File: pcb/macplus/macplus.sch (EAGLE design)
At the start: 9 parts, among them J1 ATX24RH

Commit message: mac plus adaptor pretty much done
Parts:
- added JP3: (no value), pinhead:PINHD-1X2
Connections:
- net GND: now also JP3.2
- net N$10: now also JP3.1
- net N$6: no longer J1.5V@0
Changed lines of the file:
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@@
 <part name="P+5" library="supply1" library_urn="urn:adsk.eagle:library:371" deviceset="+12V" device=""/>
 <part name="P+6" library="supply1" library_urn="urn:adsk.eagle:library:371" deviceset="+5V" device=""/>
+<part name="JP3" library="pinhead" library_urn="urn:adsk.eagle:library:325" deviceset="PINHD-1X2" device="" package3d_urn="urn:adsk.eagle:package:22435/2"/>
+<part name="GND5" library="supply1" library_urn="urn:adsk.eagle:library:371" deviceset="GND" device=""/>
 </parts>
 <sheets>
@@
 <attribute name="VALUE" x="22.86" y="96.52" size="1.778" layer="96" rot="R90"/>
 </instance>
+<instance part="JP3" gate="G$1" x="165.1" y="78.74" smashed="yes">
+<attribute name="NAME" x="158.75" y="84.455" size="1.778" layer="95"/>
+<attribute name="VALUE" x="158.75" y="73.66" size="1.778" layer="96"/>
+</instance>
+<instance part="GND5" gate="1" x="177.8" y="73.66" smashed="yes">
+<attribute name="VALUE" x="175.26" y="71.12" size="1.778" layer="96"/>
+</instance>
 </instances>
 <busses>
@@
 <pinref part="U$3" gate="G$1" pin="11_VBATT"/>
 <wire x1="43.18" y1="81.28" x2="116.84" y2="81.28" width="0.1524" layer="91"/>
+<pinref part="JP3" gate="G$1" pin="1"/>
+<wire x1="116.84" y1="81.28" x2="162.56" y2="81.28" width="0.1524" layer="91"/>
+<junction x="116.84" y="81.28"/>
 </segment>
 </net>
@@
 <wire x1="-17.78" y1="99.06" x2="-27.94" y2="99.06" width="0.1524" layer="91"/>
 </segment>
+<segment>
+<pinref part="GND5" gate="1" pin="GND"/>
+<pinref part="JP3" gate="G$1" pin="2"/>
+<wire x1="177.8" y1="76.2" x2="177.8" y2="78.74" width="0.1524" layer="91"/>
+<wire x1="177.8" y1="78.74" x2="162.56" y2="78.74" width="0.1524" layer="91"/>
+</segment>
 </net>
 <net name="-12V" class="0">
@@
 <wire x1="68.58" y1="185.42" x2="68.58" y2="187.96" width="0.1524" layer="91"/>
 <junction x="68.58" y="187.96"/>
-<pinref part="J1" gate="G$1" pin="5V@0"/>
-<wire x1="81.28" y1="182.88" x2="68.58" y2="182.88" width="0.1524" layer="91"/>
-<wire x1="68.58" y1="182.88" x2="68.58" y2="185.42" width="0.1524" layer="91"/>
-<junction x="68.58" y="185.42"/>
 <pinref part="U$8" gate="G$1" pin="B0"/>
 <pinref part="U$8" gate="G$1" pin="B1"/>

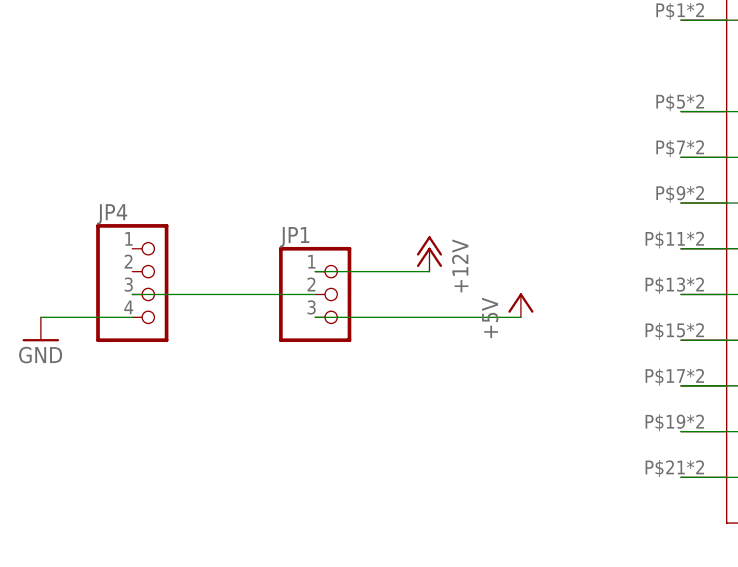
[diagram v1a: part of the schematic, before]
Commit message: updated mac plus atx adaptor
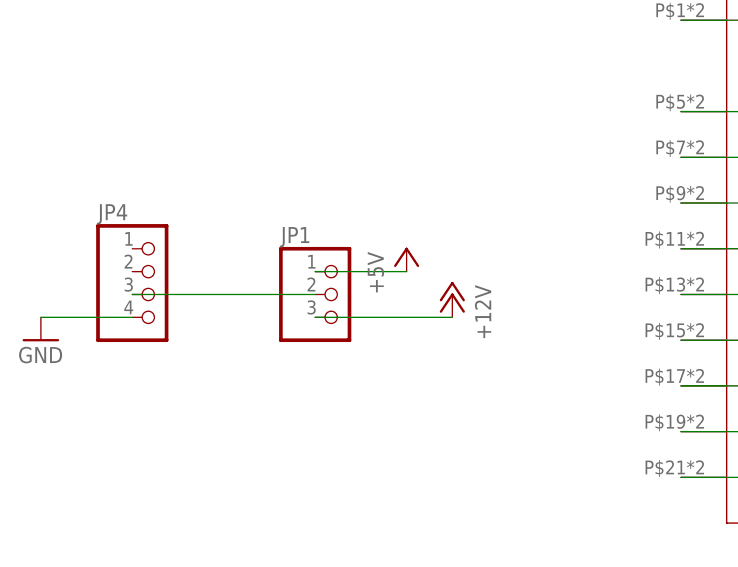
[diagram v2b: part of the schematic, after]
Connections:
- net +12V: now also JP1.3; no longer JP1.1
- net +5V: now also JP1.1; no longer JP1.3
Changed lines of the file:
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@@
 <part name="U$8" library="atx_power_control" deviceset="CAR_FUSE_HOLDER" device="3IN1"/>
 <part name="U$2" library="atx_power_control" deviceset="CAR_FUSE_HOLDER" device="3IN1"/>
-<part name="JP1" library="pinhead" library_urn="urn:adsk.eagle:library:325" deviceset="PINHD-1X3" device="" package3d_urn="urn:adsk.eagle:package:22458/2"/>
 <part name="JP2" library="pinhead" library_urn="urn:adsk.eagle:library:325" deviceset="PINHD-1X2" device="" package3d_urn="urn:adsk.eagle:package:22435/2"/>
 <part name="P+3" library="supply1" library_urn="urn:adsk.eagle:library:371" deviceset="+5V" device=""/>
@@
 <part name="JP3" library="pinhead" library_urn="urn:adsk.eagle:library:325" deviceset="PINHD-1X2" device="" package3d_urn="urn:adsk.eagle:package:22435/2"/>
 <part name="GND5" library="supply1" library_urn="urn:adsk.eagle:library:371" deviceset="GND" device=""/>
+<part name="JP1" library="pinhead" library_urn="urn:adsk.eagle:library:325" deviceset="PINHD-1X3" device="" package3d_urn="urn:adsk.eagle:package:22458/2"/>
 </parts>
 <sheets>
@@
 <instance part="U$8" gate="G$1" x="38.1" y="187.96" smashed="yes"/>
 <instance part="U$2" gate="G$1" x="154.94" y="175.26" smashed="yes"/>
+<instance part="JP2" gate="G$1" x="180.34" y="160.02" smashed="yes">
+<attribute name="NAME" x="173.99" y="165.735" size="1.778" layer="95"/>
+<attribute name="VALUE" x="173.99" y="154.94" size="1.778" layer="96"/>
+</instance>
+<instance part="P+3" gate="1" x="12.7" y="193.04" smashed="yes">
+<attribute name="VALUE" x="10.16" y="187.96" size="1.778" layer="96" rot="R90"/>
+</instance>
+<instance part="P+1" gate="1" x="175.26" y="88.9" smashed="yes" rot="MR0">
+<attribute name="VALUE" x="177.8" y="83.82" size="1.778" layer="96" rot="MR90"/>
+</instance>
+<instance part="P-2" gate="1" x="149.86" y="93.98" smashed="yes" rot="MR0">
+<attribute name="VALUE" x="152.4" y="91.44" size="1.778" layer="96" rot="MR90"/>
+</instance>
+<instance part="P+4" gate="1" x="149.86" y="109.22" smashed="yes">
+<attribute name="VALUE" x="147.32" y="104.14" size="1.778" layer="96" rot="R90"/>
+</instance>
+<instance part="GND3" gate="1" x="149.86" y="157.48" smashed="yes">
+<attribute name="VALUE" x="147.32" y="154.94" size="1.778" layer="96"/>
+</instance>
+<instance part="GND4" gate="1" x="-27.94" y="96.52" smashed="yes">
+<attribute name="VALUE" x="-30.48" y="93.98" size="1.778" layer="96"/>
+</instance>
+<instance part="P+5" gate="1" x="17.78" y="101.6" smashed="yes" rot="MR0">
+<attribute name="VALUE" x="20.32" y="96.52" size="1.778" layer="96" rot="MR90"/>
+</instance>
+<instance part="P+6" gate="1" x="12.7" y="106.68" smashed="yes">
+<attribute name="VALUE" x="10.16" y="101.6" size="1.778" layer="96" rot="R90"/>
+</instance>
+<instance part="JP3" gate="G$1" x="165.1" y="78.74" smashed="yes">
+<attribute name="NAME" x="158.75" y="84.455" size="1.778" layer="95"/>
+<attribute name="VALUE" x="158.75" y="73.66" size="1.778" layer="96"/>
+</instance>
+<instance part="GND5" gate="1" x="177.8" y="73.66" smashed="yes">
+<attribute name="VALUE" x="175.26" y="71.12" size="1.778" layer="96"/>
+</instance>
 <instance part="JP1" gate="A" x="5.08" y="101.6" smashed="yes">
 <attribute name="NAME" x="-1.27" y="107.315" size="1.778" layer="95"/>
 <attribute name="VALUE" x="-1.27" y="93.98" size="1.778" layer="96"/>
-</instance>
-<instance part="JP2" gate="G$1" x="180.34" y="160.02" smashed="yes">
-<attribute name="NAME" x="173.99" y="165.735" size="1.778" layer="95"/>
-<attribute name="VALUE" x="173.99" y="154.94" size="1.778" layer="96"/>
-</instance>
-<instance part="P+3" gate="1" x="12.7" y="193.04" smashed="yes">
-<attribute name="VALUE" x="10.16" y="187.96" size="1.778" layer="96" rot="R90"/>
-</instance>
-<instance part="P+1" gate="1" x="175.26" y="88.9" smashed="yes" rot="MR0">
-<attribute name="VALUE" x="177.8" y="83.82" size="1.778" layer="96" rot="MR90"/>
-</instance>
-<instance part="P-2" gate="1" x="149.86" y="93.98" smashed="yes" rot="MR0">
-<attribute name="VALUE" x="152.4" y="91.44" size="1.778" layer="96" rot="MR90"/>
-</instance>
-<instance part="P+4" gate="1" x="149.86" y="109.22" smashed="yes">
-<attribute name="VALUE" x="147.32" y="104.14" size="1.778" layer="96" rot="R90"/>
-</instance>
-<instance part="GND3" gate="1" x="149.86" y="157.48" smashed="yes">
-<attribute name="VALUE" x="147.32" y="154.94" size="1.778" layer="96"/>
-</instance>
-<instance part="GND4" gate="1" x="-27.94" y="96.52" smashed="yes">
-<attribute name="VALUE" x="-30.48" y="93.98" size="1.778" layer="96"/>
-</instance>
-<instance part="P+5" gate="1" x="15.24" y="106.68" smashed="yes" rot="MR0">
-<attribute name="VALUE" x="17.78" y="101.6" size="1.778" layer="96" rot="MR90"/>
-</instance>
-<instance part="P+6" gate="1" x="25.4" y="101.6" smashed="yes">
-<attribute name="VALUE" x="22.86" y="96.52" size="1.778" layer="96" rot="R90"/>
-</instance>
-<instance part="JP3" gate="G$1" x="165.1" y="78.74" smashed="yes">
-<attribute name="NAME" x="158.75" y="84.455" size="1.778" layer="95"/>
-<attribute name="VALUE" x="158.75" y="73.66" size="1.778" layer="96"/>
-</instance>
-<instance part="GND5" gate="1" x="177.8" y="73.66" smashed="yes">
-<attribute name="VALUE" x="175.26" y="71.12" size="1.778" layer="96"/>
 </instance>
 </instances>
@@
 </segment>
 <segment>
-<pinref part="JP1" gate="A" pin="3"/>
+<pinref part="JP1" gate="A" pin="1"/>
 <pinref part="P+6" gate="1" pin="+5V"/>
-<wire x1="2.54" y1="99.06" x2="25.4" y2="99.06" width="0.1524" layer="91"/>
+<wire x1="2.54" y1="104.14" x2="12.7" y2="104.14" width="0.1524" layer="91"/>
 </segment>
 </net>
@@
 <segment>
 <pinref part="P+5" gate="1" pin="+12V"/>
-<pinref part="JP1" gate="A" pin="1"/>
-<wire x1="15.24" y1="104.14" x2="2.54" y2="104.14" width="0.1524" layer="91"/>
+<pinref part="JP1" gate="A" pin="3"/>
+<wire x1="17.78" y1="99.06" x2="2.54" y2="99.06" width="0.1524" layer="91"/>
 </segment>
 </net>
@@
 <net name="N$7" class="0">
 <segment>
+<pinref part="JP4" gate="A" pin="3"/>
 <pinref part="JP1" gate="A" pin="2"/>
-<pinref part="JP4" gate="A" pin="3"/>
-<wire x1="2.54" y1="101.6" x2="-17.78" y2="101.6" width="0.1524" layer="91"/>
-</segment>
-</net>
+<wire x1="-17.78" y1="101.6" x2="2.54" y2="101.6" width="0.1524" layer="91"/>
+</segment>
+</net>

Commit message: finishing touches
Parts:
- added C2: (no value), capacitor-wima:C5/2.5
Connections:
- net +12V: now also C2.1
- net GND: now also C2.2
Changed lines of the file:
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@@
 <part name="GND5" library="supply1" library_urn="urn:adsk.eagle:library:371" deviceset="GND" device=""/>
 <part name="JP1" library="pinhead" library_urn="urn:adsk.eagle:library:325" deviceset="PINHD-1X3" device="" package3d_urn="urn:adsk.eagle:package:22458/2"/>
+<part name="C2" library="capacitor-wima" library_urn="urn:adsk.eagle:library:116" deviceset="C" device="5/2.5" package3d_urn="urn:adsk.eagle:package:5426/1"/>
+<part name="P+7" library="supply1" library_urn="urn:adsk.eagle:library:371" deviceset="+12V" device=""/>
+<part name="GND6" library="supply1" library_urn="urn:adsk.eagle:library:371" deviceset="GND" device=""/>
 </parts>
 <sheets>
@@
 <attribute name="NAME" x="-1.27" y="107.315" size="1.778" layer="95"/>
 <attribute name="VALUE" x="-1.27" y="93.98" size="1.778" layer="96"/>
+</instance>
+<instance part="C2" gate="G$1" x="7.62" y="144.78" smashed="yes">
+<attribute name="NAME" x="9.144" y="145.161" size="1.778" layer="95"/>
+<attribute name="VALUE" x="9.144" y="140.081" size="1.778" layer="96"/>
+</instance>
+<instance part="P+7" gate="1" x="7.62" y="149.86" smashed="yes" rot="MR0">
+<attribute name="VALUE" x="10.16" y="144.78" size="1.778" layer="96" rot="MR90"/>
+</instance>
+<instance part="GND6" gate="1" x="7.62" y="137.16" smashed="yes">
+<attribute name="VALUE" x="5.08" y="134.62" size="1.778" layer="96"/>
 </instance>
 </instances>
@@
 <wire x1="177.8" y1="78.74" x2="162.56" y2="78.74" width="0.1524" layer="91"/>
 </segment>
+<segment>
+<pinref part="C2" gate="G$1" pin="2"/>
+<pinref part="GND6" gate="1" pin="GND"/>
+</segment>
 </net>
 <net name="-12V" class="0">
@@
 <wire x1="17.78" y1="99.06" x2="2.54" y2="99.06" width="0.1524" layer="91"/>
 </segment>
-</net>
+<segment>
+<pinref part="C2" gate="G$1" pin="1"/>
+<pinref part="P+7" gate="1" pin="+12V"/>
+</segment>
+</net>
